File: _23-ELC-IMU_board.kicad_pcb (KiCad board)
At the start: 2 copper layers, 71 parts, among them J1 Deutsch DT6, J2 Deutsch DT6, J3 Conn_01x03, J4 Conn_01x02, J5 SWD, SW1 SW_SPDT, U1 LSM6DSR, U2 STM32F105RCTx, U3 SN65HVD230, U4 CD143A-SR05, U5 TPS562200, U6 AMS1117-3.3, Y1 16MHz

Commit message: Good enough
Will make a ground plane next time
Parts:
- moved H2 135.3 mm to (127.0, 114.3)
- moved H3 108.2 mm to (127.6, 149.9)
- moved H4 99.6 mm to (177.8, 149.9)
- moved U6 32.8 mm to (148.0, 142.3), turned to -90 degrees
- moved C22 28.3 mm to (146.3, 136.5), turned to 0 degrees
- moved R18 26.9 mm to (141.6, 145.4), turned to 0 degrees
- moved F1 25.1 mm to (145.2, 133.3), turned to 0 degrees
- moved C18 23.7 mm to (137.2, 145.4), turned to 180 degrees
- moved L1 23.3 mm to (140.3, 140.9), turned to 0 degrees
- moved C21 22.9 mm to (141.8, 136.5), turned to 180 degrees
- moved R17 21.3 mm to (132.7, 145.4), turned to 180 degrees
- moved TP3 20.5 mm to (137.8, 123.7)
- moved C15 20.0 mm to (131.4, 142.2)
- moved U5 19.1 mm to (134.6, 140.9), turned to -90 degrees
- moved C20 18.8 mm to (138.7, 135.9), turned to 90 degrees
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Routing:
- net +3V3: track 179.5 -> 157.9 mm
- net GND: track 224.4 -> 242.1 mm, vias 3 -> 6
- net Net-(C10-Pad1): track 19.3 -> 32.4 mm
- net /CALIB_BUTTON: track 7.10 -> 18.4 mm
- net Net-(C11-Pad1): track 27.7 -> 37.7 mm, vias 0 -> 1
- net /VRMS/BUCK/V_in: track 18.4 -> 26.6 mm
- net +5V: track 27.0 -> 34.8 mm, vias 0 -> 2
- net /VRMS/BUCK/EN: track 4.50 -> 5.69 mm
- net /VRMS/BUCK/SW: track 9.33 -> 8.15 mm
- net Net-(C12-Pad2): track 8.74 -> 9.58 mm
- net Net-(J4-Pad2): track 6.06 -> 6.79 mm

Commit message: PCB adjustments
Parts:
- moved H1 147.8 mm to (161.3, 118.1)
- moved H2 10.8 mm to (127.6, 125.1)
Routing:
- net GND: track 242.1 -> 267.3 mm
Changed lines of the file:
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@@
   )
   (footprint "MountingHole:MountingHole_3.5mm_Pad" (layer "F.Cu")
-    (at 127 114.3)
+    (at 127.635 125.095)
     (descr "Mounting Hole 3.5mm")
     (tags "mounting hole 3.5mm")
@@
   )
   (footprint "MountingHole:MountingHole_3.5mm_Pad" (layer "F.Cu")
-    (at 274.32 22.86)
+    (at 161.29 118.11)
     (descr "Mounting Hole 3.5mm")
     (tags "mounting hole 3.5mm")
@@
   (via (at 167.005 138.43) (size 0.8) (drill 0.4) (layers "F.Cu" "B.Cu") (net 2))
   (via (at 135.255 138.43) (size 0.8) (drill 0.4) (layers "F.Cu" "B.Cu") (net 2))
+  (segment (start 161.29 118.11) (end 162.555 118.11) (width 0.25) (layer "B.Cu") (net 2))
   (segment (start 178.435 125.73) (end 179.751469 127.046469) (width 0.25) (layer "B.Cu") (net 2))
+  (segment (start 162.555 118.11) (end 167.635 123.19) (width 0.25) (layer "B.Cu") (net 2))
+  (segment (start 127.635 125.095) (end 127.635 136.525) (width 0.25) (layer "B.Cu") (net 2))
   (segment (start 167.155 138.43) (end 173.43 144.705) (width 0.25) (layer "B.Cu") (net 2))
   (segment (start 170.815 121.285) (end 172.085 122.555) (width 0.25) (layer "B.Cu") (net 2))
@@
   (segment (start 167.005 138.43) (end 167.155 138.43) (width 0.25) (layer "B.Cu") (net 2))
   (segment (start 179.751469 127.046469) (end 179.751469 132.033531) (width 0.25) (layer "B.Cu") (net 2))
+  (segment (start 127.635 136.525) (end 131.445 140.335) (width 0.25) (layer "B.Cu") (net 2))
   (segment (start 162.56 144.78) (end 164.465 144.78) (width 0.25) (layer "B.Cu") (net 2))
   (segment (start 167.635 123.19) (end 169.54 121.285) (width 0.25) (layer "B.Cu") (net 2))

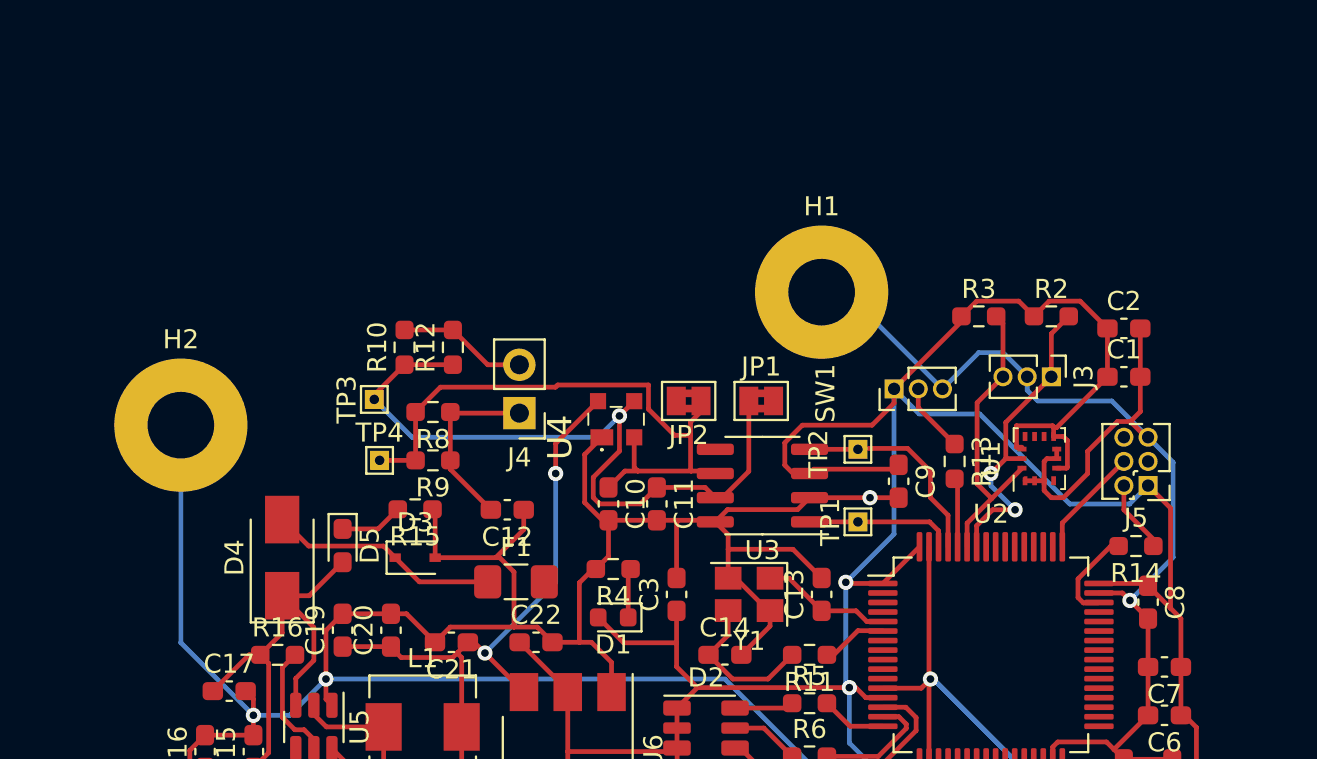
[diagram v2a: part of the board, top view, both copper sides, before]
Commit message: Moved the mounting holes
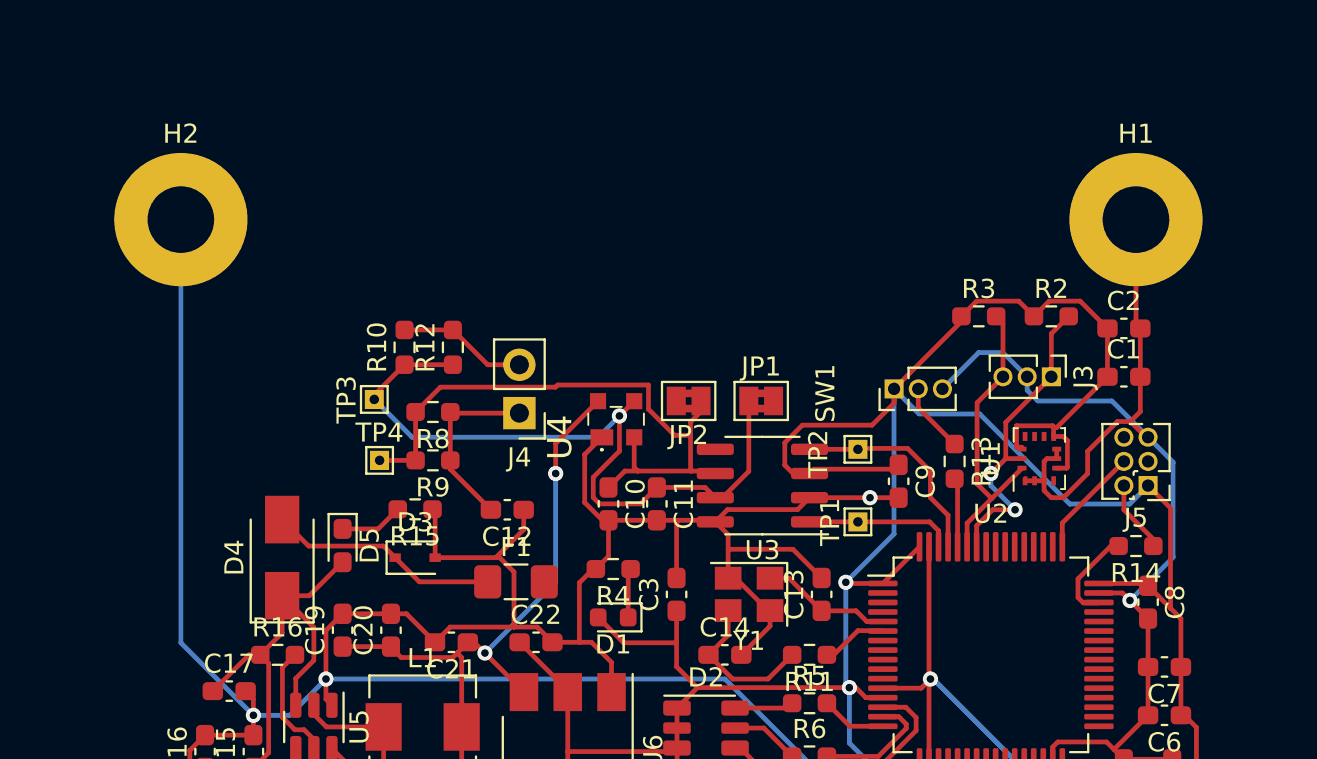
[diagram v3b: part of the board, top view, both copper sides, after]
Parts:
- moved H1 16.9 mm to (177.8, 114.3)
- moved H2 10.8 mm to (127.6, 114.3)
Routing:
- net GND: track 267.3 -> 275.5 mm
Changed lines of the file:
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@@
   )
   (footprint "MountingHole:MountingHole_3.5mm_Pad" (layer "F.Cu")
-    (at 127.635 125.095)
+    (at 127.635 114.3)
     (descr "Mounting Hole 3.5mm")
     (tags "mounting hole 3.5mm")
@@
   )
   (footprint "MountingHole:MountingHole_3.5mm_Pad" (layer "F.Cu")
-    (at 161.29 118.11)
+    (at 177.8 114.3)
     (descr "Mounting Hole 3.5mm")
     (tags "mounting hole 3.5mm")
@@
   (segment (start 177.506727 124.905) (end 176.823273 124.905) (width 0.25) (layer "F.Cu") (net 2))
   (segment (start 145.6425 129.54) (end 145.6425 130.5825) (width 0.25) (layer "F.Cu") (net 2))
+  (segment (start 177.8 119.7875) (end 178.0275 120.015) (width 0.25) (layer "F.Cu") (net 2))
   (segment (start 157.0725 137.16) (end 158.58 135.6525) (width 0.25) (layer "F.Cu") (net 2))
   (segment (start 128.105 142.1775) (end 128.905 141.3775) (width 0.25) (layer "F.Cu") (net 2))
@@
   (segment (start 144.17 132.055) (end 144.380672 132.055) (width 0.25) (layer "F.Cu") (net 2))
   (segment (start 164.505 138.91) (end 166.525 138.91) (width 0.25) (layer "F.Cu") (net 2))
+  (segment (start 177.8 114.3) (end 177.8 119.7875) (width 0.25) (layer "F.Cu") (net 2))
   (segment (start 173.43 144.705) (end 173.43 142.835) (width 0.25) (layer "F.Cu") (net 2))
   (segment (start 159.7825 131.615) (end 156.38 131.615) (width 0.25) (layer "F.Cu") (net 2))
@@
   (via (at 167.005 138.43) (size 0.8) (drill 0.4) (layers "F.Cu" "B.Cu") (net 2))
   (via (at 135.255 138.43) (size 0.8) (drill 0.4) (layers "F.Cu" "B.Cu") (net 2))
-  (segment (start 161.29 118.11) (end 162.555 118.11) (width 0.25) (layer "B.Cu") (net 2))
   (segment (start 178.435 125.73) (end 179.751469 127.046469) (width 0.25) (layer "B.Cu") (net 2))
-  (segment (start 162.555 118.11) (end 167.635 123.19) (width 0.25) (layer "B.Cu") (net 2))
-  (segment (start 127.635 125.095) (end 127.635 136.525) (width 0.25) (layer "B.Cu") (net 2))
   (segment (start 167.155 138.43) (end 173.43 144.705) (width 0.25) (layer "B.Cu") (net 2))
   (segment (start 170.815 121.285) (end 172.085 122.555) (width 0.25) (layer "B.Cu") (net 2))
+  (segment (start 127.635 114.3) (end 127.635 136.525) (width 0.25) (layer "B.Cu") (net 2))
   (segment (start 178.435 125.73) (end 176.53 123.825) (width 0.25) (layer "B.Cu") (net 2))
   (segment (start 176.53 123.825) (end 172.647894 123.825) (width 0.25) (layer "B.Cu") (net 2))
@@
   (segment (start 167.005 138.28) (end 173.43 144.705) (width 0.25) (layer "B.Cu") (net 2))
   (segment (start 172.647894 123.825) (end 172.085 123.262106) (width 0.25) (layer "B.Cu") (net 2))
+  (segment (start 127.635 136.525) (end 131.445 140.335) (width 0.25) (layer "B.Cu") (net 2))
   (segment (start 169.54 121.285) (end 170.815 121.285) (width 0.25) (layer "B.Cu") (net 2))
   (segment (start 133.35 140.335) (end 135.255 138.43) (width 0.25) (layer "B.Cu") (net 2))
@@
   (segment (start 167.005 138.43) (end 167.155 138.43) (width 0.25) (layer "B.Cu") (net 2))
   (segment (start 179.751469 127.046469) (end 179.751469 132.033531) (width 0.25) (layer "B.Cu") (net 2))
-  (segment (start 127.635 136.525) (end 131.445 140.335) (width 0.25) (layer "B.Cu") (net 2))
   (segment (start 162.56 144.78) (end 164.465 144.78) (width 0.25) (layer "B.Cu") (net 2))
   (segment (start 167.635 123.19) (end 169.54 121.285) (width 0.25) (layer "B.Cu") (net 2))
